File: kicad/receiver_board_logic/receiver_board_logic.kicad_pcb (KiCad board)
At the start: 2 copper layers, 31 x 63 mm, 11 parts, among them J1 B2B, J2 Motor 1, J3 Motor 2, Q1 FQP27P06, SW2 Pair/Direction, U4 Dual H Bridge, U5 ESP32-C3-SuperMini

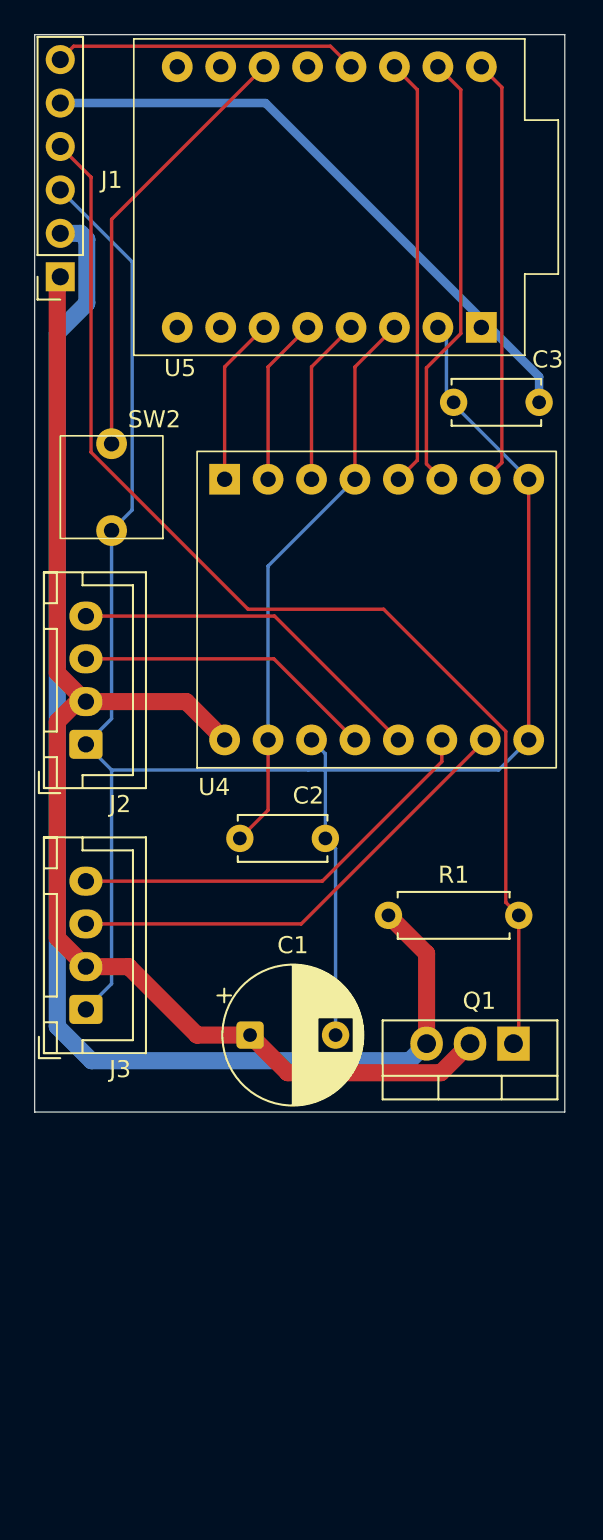
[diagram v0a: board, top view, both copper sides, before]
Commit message: Remove BMS and reorganize receiver boards for external charging
Major schematic and layout revision based on EE review:

- Remove BMS from receiver design; pivot to external LiPo charging
- Reorganize components between power and logic boards:
  - Logic board: P-FET power switch, buck converter, UI (LED/button), debug UART
  - Power board: ESP32-C3, motor driver, battery monitoring
- Add voltage dividers for 2S LiPo monitoring (B+ and BM)
  - Safe ADC voltages: B+ = 2.36V max, BM = 2.47V max
- Add debug UART headers (GPIO20/21) for serial output when USB unavailable
- Fix P-FET drain connection to properly power both buck and motor system
- Update B2B connectors to dual 6-pin configuration (signal + power)
- Minor controller board PCB layout adjustments

Co-Authored-By: Claude Sonnet 4.5 <noreply@anthropic.com>
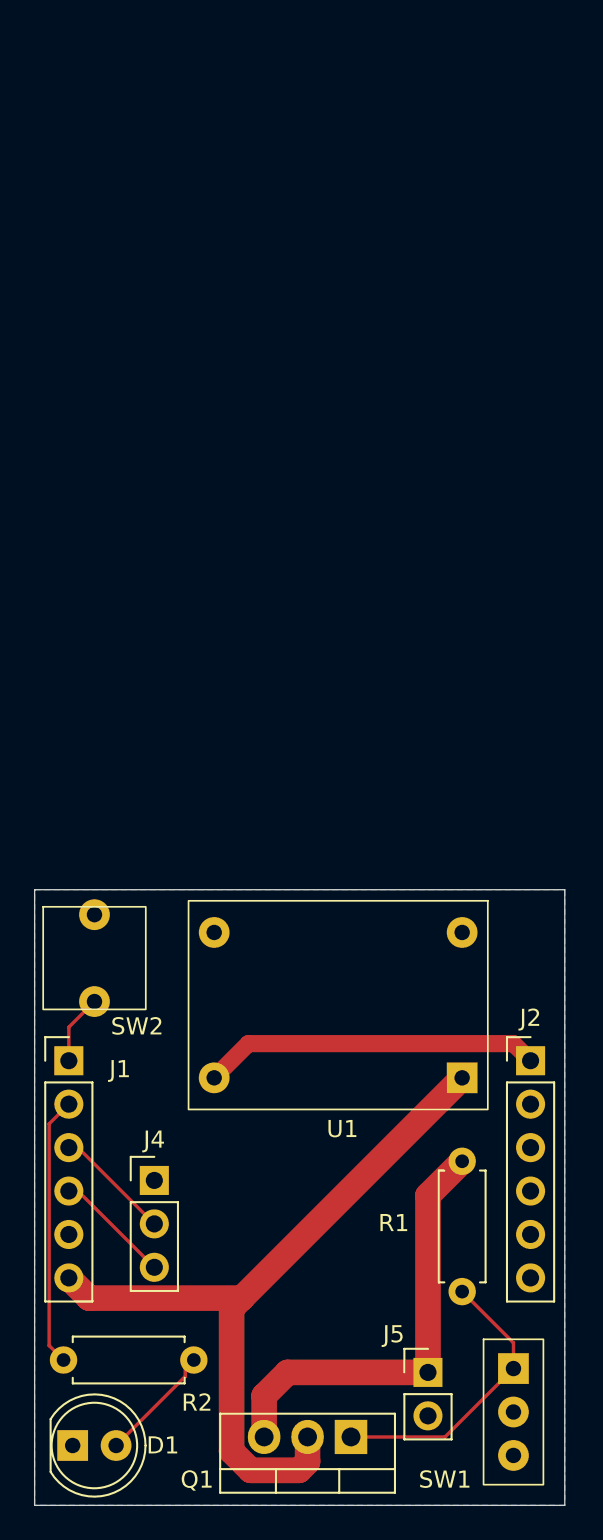
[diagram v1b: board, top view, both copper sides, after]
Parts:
- removed C1: 470uF, Capacitor_THT:CP_Radial_D8.0mm_P5.00mm
- removed C2, C3: 0.1uF, Capacitor_THT:C_Disc_D5.0mm_W2.5mm_P5.00mm
- removed J3: Motor 2, Connector_JST:JST_XH_B4B-XH-A_1x04_P2.50mm_Vertical
- removed U4: Dual H Bridge, ESP32_Lego_PF:TB6612FNG
- removed U5: ESP32-C3-SuperMini, ESP32_Lego_PF:ESP32-C3-SuperMini
- added D1: Status, LED_THT:LED_D5.0mm, F.Cu at (102.2, 132.5)
- added J4: Debug, Connector_PinHeader_2.54mm:PinHeader_1x03_P2.54mm_Vertical, F.Cu at (107.0, 117.0)
- added J5: Battery Conn, Connector_PinHeader_2.54mm:PinHeader_1x02_P2.54mm_Vertical, F.Cu at (123.0, 128.2)
- added R2: 1k, Resistor_THT:R_Axial_DIN0207_L6.3mm_D2.5mm_P7.62mm_Horizontal, F.Cu at (109.3, 127.5)
- added SW1: On/Off, ESP32_Lego_PF:Slide_Switch_SPDT_12D00G, F.Cu at (128.0, 130.5)
- added U1: 5V Buck, ESP32_Lego_PF:MP1584EN, F.Cu at (117.8, 106.8)
- J1: value B2B -> B2B 1; footprint Connector_PinSocket_2.54mm:PinSocket_1x06_P2.54mm_Vertical -> Connector_PinHeader_2.54mm:PinHeader_1x06_P2.54mm_Vertical
- J2: value Motor 1 -> B2B 2; footprint Connector_JST:JST_XH_B4B-XH-A_1x04_P2.50mm_Vertical -> Connector_PinHeader_2.54mm:PinHeader_1x06_P2.54mm_Vertical
- moved J1 45.8 mm to (102.0, 110.0), turned to 0 degrees
- moved J2 31.9 mm to (129.0, 110.0), turned to 0 degrees
- moved SW2 27.6 mm to (103.5, 104.0), turned to 0 degrees
- moved Q1 24.9 mm to (118.5, 132.0)
- moved R1 15.0 mm to (125.0, 115.9), turned to -90 degrees
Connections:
- J1 pad 1: /7v4_FET -> /BUT_ESP
- J1 pad 2: /7v4_BMS -> /LED_ESP
- J1 pad 3: /GND -> /TX
- J1 pad 4: /PWR_SW -> /RX
- J1 pad 5: /5v_BUCK -> /GND
- J1 pad 6: /LED_ESP -> /7v4_FET
- J2 pad 1: /GND -> /5v_BUCK
- J2 pad 2: /7v4_FET -> /GND
- J2 pad 3: /MOT1_C1 -> /GND
- J2 pad 4: /MOT1_C2 -> /GND
- Q1 pad 3: /7v4_BMS -> Net-(J5-Pin_1)
- R1 pad 1: /7v4_BMS -> Net-(J5-Pin_1)
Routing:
- net /GND: track 121.1 -> 0.00 mm
- net /7v4_BMS: track 79.7 -> 0.00 mm
- net /PWR_SW: track 68.3 -> 16.9 mm
- net /3v3_ESP: track 33.6 -> 0.00 mm
- net /7v4_FET: track 77.6 -> 44.6 mm
- net /MOT2_C1: track 27.8 -> 0.00 mm
- net /MOT2_IN2: track 25.9 -> 0.00 mm
- net Net-(J5-Pin_1): track 0.00 -> 25.8 mm
- net /MOT2_IN1: track 25.1 -> 0.00 mm
- net /MOT2_PWM: track 25.0 -> 0.00 mm
- net /MOT2_C2: track 25.0 -> 0.00 mm
- net /BUT_ESP: track 25.7 -> 4.08 mm
- net /MOT1_C2: track 21.3 -> 0.00 mm
- net /MOT1_C1: track 17.7 -> 0.00 mm
- net /5v_BUCK: track 36.1 -> 19.7 mm
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- added copper zone on B.Cu, net /GND
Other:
- board size 31 x 63 mm -> 31 x 36 mm
